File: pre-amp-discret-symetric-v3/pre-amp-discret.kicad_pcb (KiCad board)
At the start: 2 copper layers, 81.9 x 52.1 mm, 66 parts, among them J1 Conn_01x01, J2 Conn_01x01, J3 Conn_01x01, J4 Conn_01x01, J5 Conn_01x01, J6 Conn_01x01, J7 Conn_01x01, Q1 BCM857DS,115, Q10 BC860C, Q11 BCM847DS,115, Q13 BCM847DS,115, Q14 BCM857DS,115, Q18 BC860C, Q19 BC860C, Q2 BCM847DS,115, Q20 BC850C, Q3 BCM857DS,115, Q6 BC850C, Q7 BC860C, Q8 BC850C, Q9 BCM857DS,115

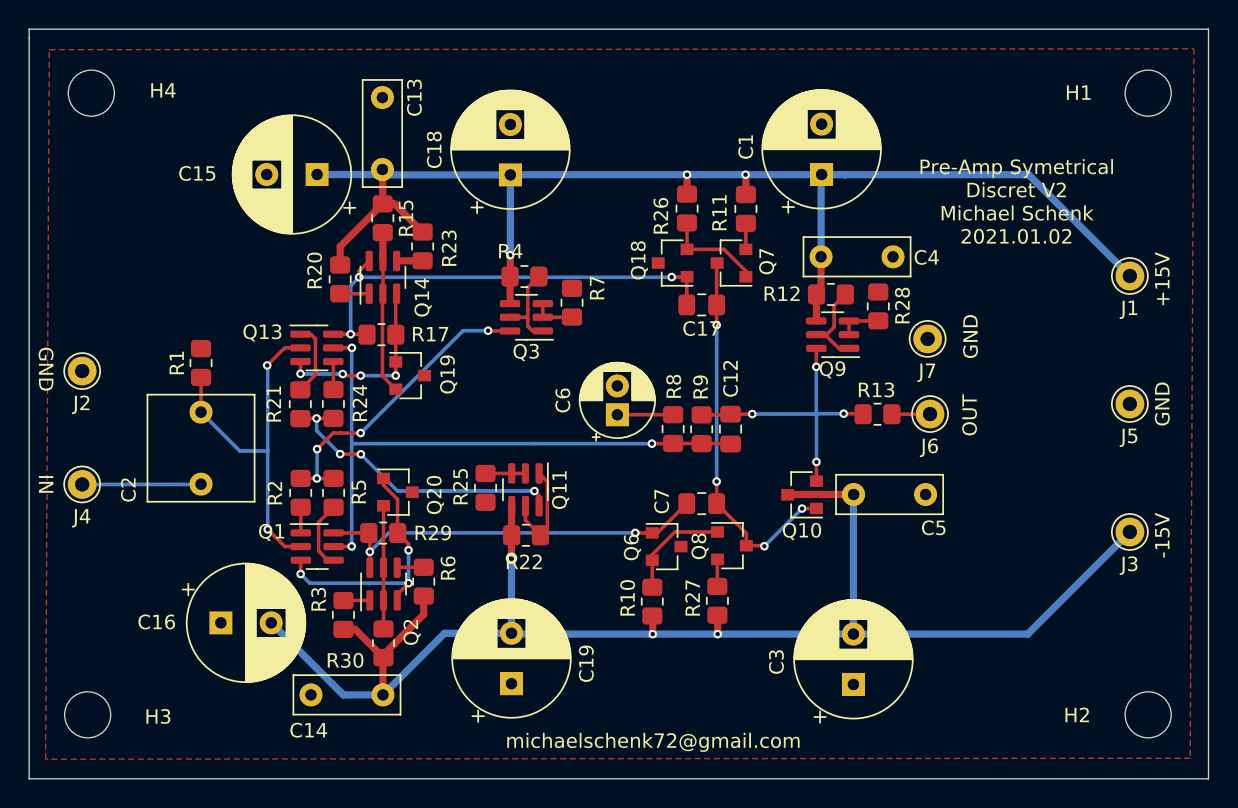
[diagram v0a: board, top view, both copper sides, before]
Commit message: First layout completed
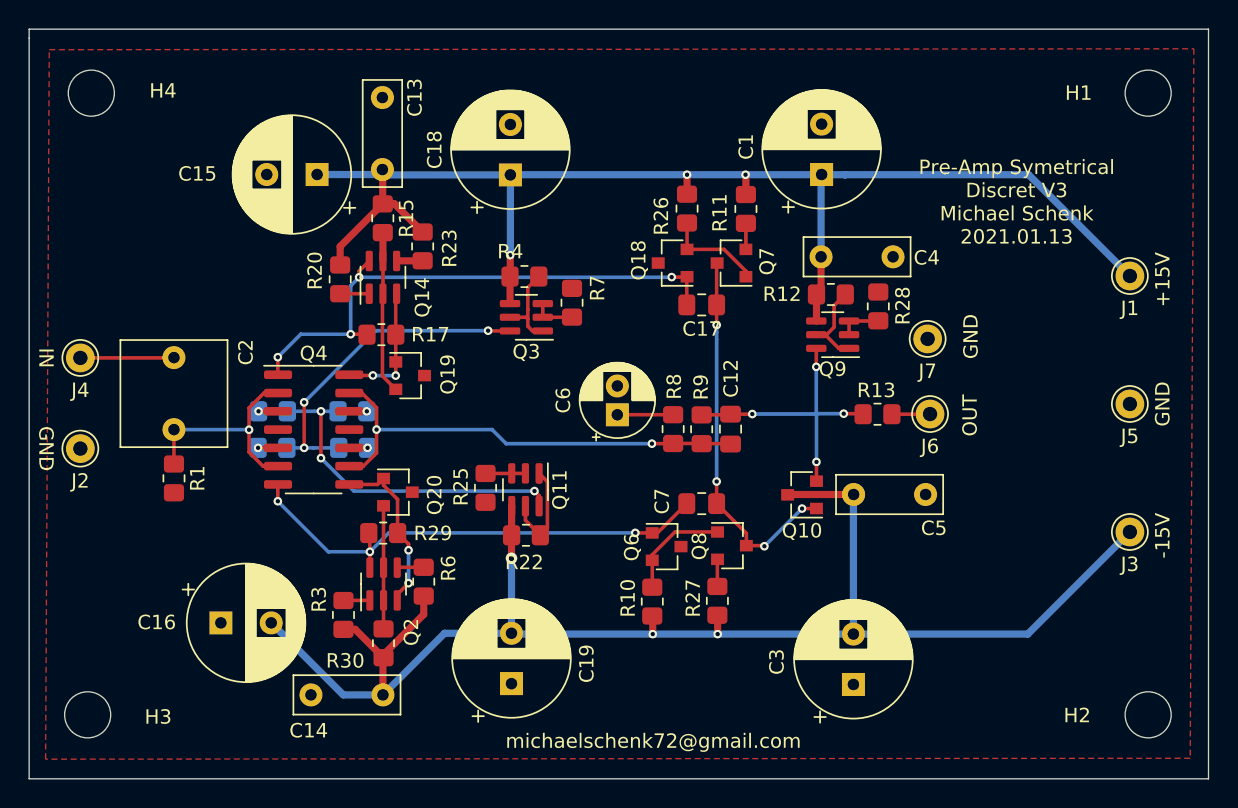
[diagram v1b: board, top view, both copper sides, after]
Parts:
- removed Q1: BCM857DS,115, Package_SO:SC-74-6_1.5x2.9mm_P0.95mm
- removed Q13: BCM847DS,115, Package_SO:SC-74-6_1.5x2.9mm_P0.95mm
- added Q4: THAT340, Package_SO:SOIC-14_3.9x8.7mm_P1.27mm, F.Cu at (141.7, 123.7)
- R2, R21, R24, R5: moved to B.Cu
- moved J4 8.79 mm to (125.5, 118.7)
- moved R1 8.23 mm to (132.0, 127.1), turned to 270 degrees
- moved J2 5.39 mm to (125.5, 125.0)
- moved R2 3.69 mm to (138.8, 125.0), turned to 180 degrees
- moved R5 3.41 mm to (144.4, 125.0), turned to 0 degrees
- moved C2 2.23 mm to (132.0, 123.7), turned to 90 degrees
- moved R21 1.96 mm to (138.9, 122.4), turned to 0 degrees
- moved R24 1.41 mm to (144.4, 122.4), turned to 180 degrees
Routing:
- net Net-(C12-Pad2): track 43.4 -> 32.7 mm, vias 3 -> 2
- net Net-(C2-Pad1): track 25.2 -> 15.5 mm, vias 2 -> 1
- net Net-(C7-Pad2): track 28.3 -> 34.9 mm, vias 2 -> 3
- net Net-(Q2-Pad3): track 18.2 -> 12.1 mm, vias 3 -> 2
- net Net-(C17-Pad2): track 32.7 -> 38.5 mm, vias 3 -> 4
- net Net-(Q14-Pad3): track 13.5 -> 8.97 mm, vias 4 -> 2
- net Net-(Q4-Pad3): track 5.14 -> 1.35 mm, vias 0 -> 1
- net Net-(Q4-Pad10): track 4.77 -> 1.27 mm, vias 0 -> 1
- net Net-(Q11-Pad6): track 21.2 -> 23.7 mm, vias 4 -> 3
- net Net-(C2-Pad2): track 8.29 -> 6.51 mm
- net Net-(Q3-Pad6): track 21.5 -> 23.1 mm, vias 4 -> 3
- net Net-(Q4-Pad12): track 1.95 -> 1.22 mm, vias 0 -> 1
- net Net-(Q4-Pad5): track 1.78 -> 1.39 mm, vias 0 -> 1
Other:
- board text added: "Pre-Amp Symetrical Discret V3 Michael Schenk 2021.01.13"
- board text removed: "Pre-Amp Symetrical Discret V2 Michael Schenk 2021.01.02"

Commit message: Small improvments
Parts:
- moved C6 4.72 mm to (166.6, 119.9)
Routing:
- net Net-(C6-Pad1): track 3.88 -> 2.73 mm
